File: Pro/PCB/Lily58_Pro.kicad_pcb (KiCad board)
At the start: 2 copper layers, 142.5 x 106.3 mm, 87 parts, among them J1 LED, J2 4PIN, J3 OLED, P1 i2c_pin, P2 i2c_pin, SW1 SW_PUSH, SW10 SW_PUSH, SW11 SW_PUSH, SW12 SW_PUSH, SW13 SW_PUSH, SW14 SW_PUSH, SW15 SW_PUSH, SW16 SW_PUSH, SW17 SW_PUSH, SW18 SW_PUSH, SW19 SW_PUSH, SW2 SW_PUSH, SW20 SW_PUSH, SW21 SW_PUSH, SW22 SW_PUSH, SW23 SW_PUSH, SW24 SW_PUSH, SW25 SW_PUSH, SW26 SW_PUSH, SW27 SW_PUSH, SW28 SW_PUSH, SW29 SW_PUSH, SW3 SW_PUSH, SW4 SW_PUSH, SW5 SW_PUSH, SW6 SW_PUSH, SW7 SW_PUSH, SW8 SW_PUSH, SW9 SW_PUSH, U1 ProMicro

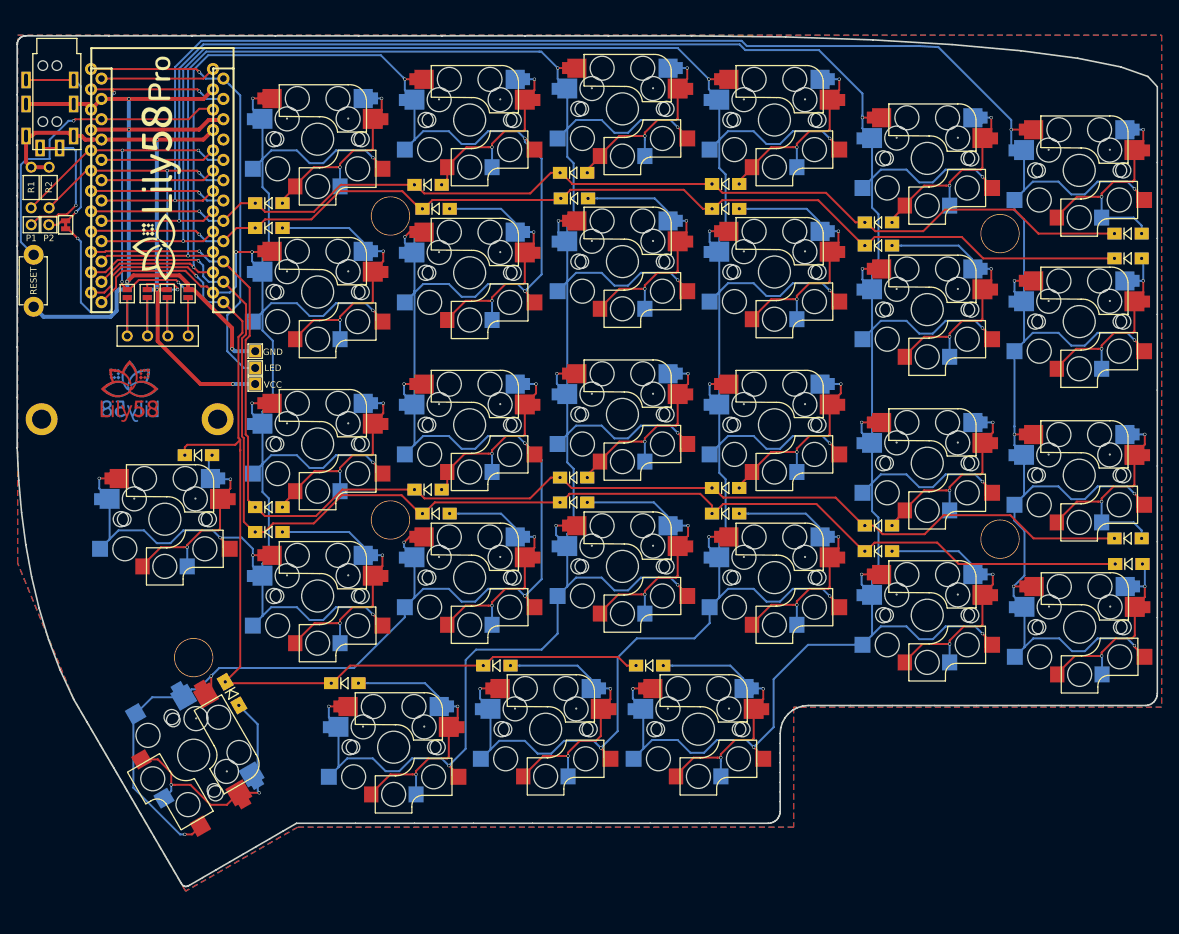
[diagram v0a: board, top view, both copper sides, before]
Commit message: Update footprints a bit, remove some DRC errors (at least we have less of the).
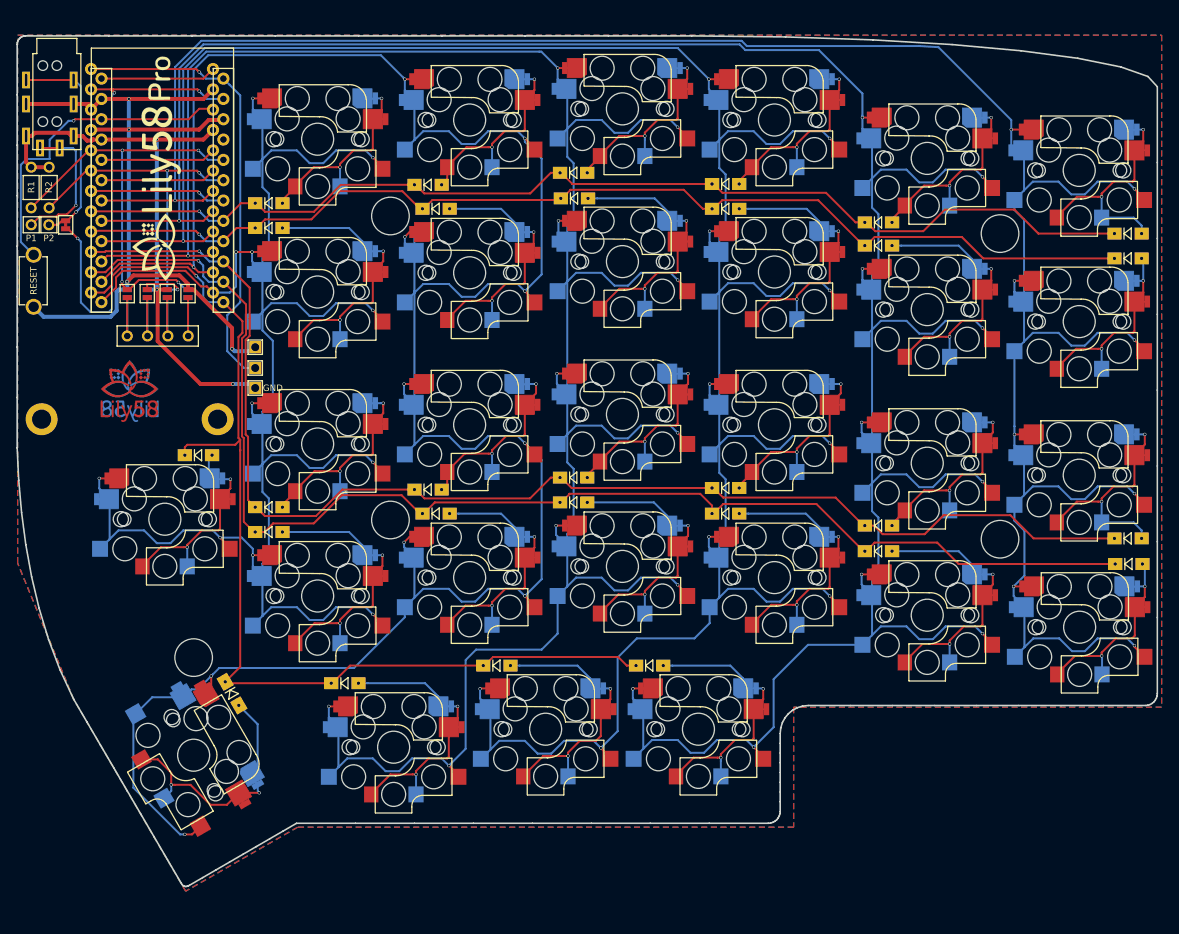
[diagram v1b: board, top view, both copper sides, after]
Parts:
- SW1, SW10, SW11, SW12, SW13, SW14, SW15, SW16, SW17, SW18, SW19, SW2, SW20, SW21, SW22, SW23, SW24, SW25, SW26, SW27, SW28, SW29, SW3, SW4, SW5, SW6, SW7, SW8, SW9: footprint Lily58-footprint:CherryMX_KailhLowProfile_Hotswap_edge -> Lily58-footprint:CherryMX_KailhLowProfile_Hotswap_edge_fixed

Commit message: Add another switch.
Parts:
- added D30: D, Lily58-footprint:Diode_SOD123, F.Cu at (180.7, 121.0)
- added SW30: SW_PUSH, Lily58-footprint:CherryMX_KailhLowProfile_Hotswap, F.Cu at (187.0, 129.0)
- SW1, SW10, SW11, SW12, SW13, SW14, SW15, SW16, SW17, SW18, SW19, SW2, SW20, SW21, SW22, SW23, SW24, SW25, SW27, SW28, SW29, SW3, SW4, SW5, SW6, SW7, SW8, SW9: footprint Lily58-footprint:CherryMX_KailhLowProfile_Hotswap_edge_fixed -> Lily58-footprint:CherryMX_KailhLowProfile_Hotswap
- SW26: footprint Lily58-footprint:CherryMX_KailhLowProfile_Hotswap_edge_fixed -> Lily58-footprint:CherryMX_KailhLowProfile_Hotswap_1.5
- moved SW26 3.22 mm to (106.0, 130.1)
- moved SW27 2.16 mm to (127.9, 126.4), turned to 15 degrees
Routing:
- net col4: track 319.5 -> 254.7 mm, vias 11 -> 10
- net col3: track 319.9 -> 260.8 mm, vias 11 -> 10
- net Net-(D27-Pad2): track 37.1 -> 4.30 mm, vias 2 -> 1
- net Net-(D26-Pad2): track 35.0 -> 4.70 mm, vias 2 -> 1
- net (no net): track 0.00 -> 4.64 mm
- net Net-(D30-Pad2): track 0.00 -> 3.84 mm, vias 0 -> 1
- net col0: track 304.4 -> 308.0 mm, vias 9 -> 10

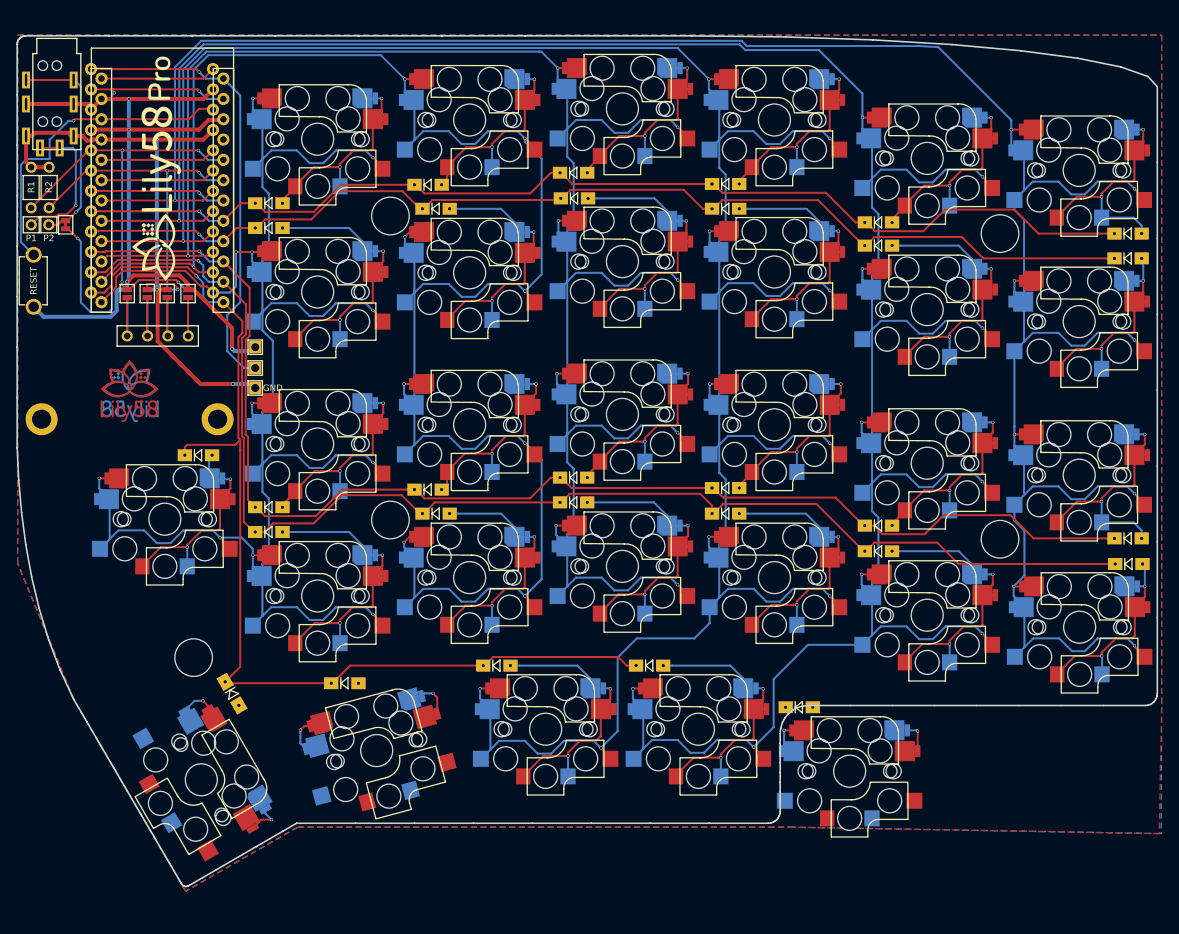
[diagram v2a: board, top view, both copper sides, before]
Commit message: Replace Edeg-Cut with new one.
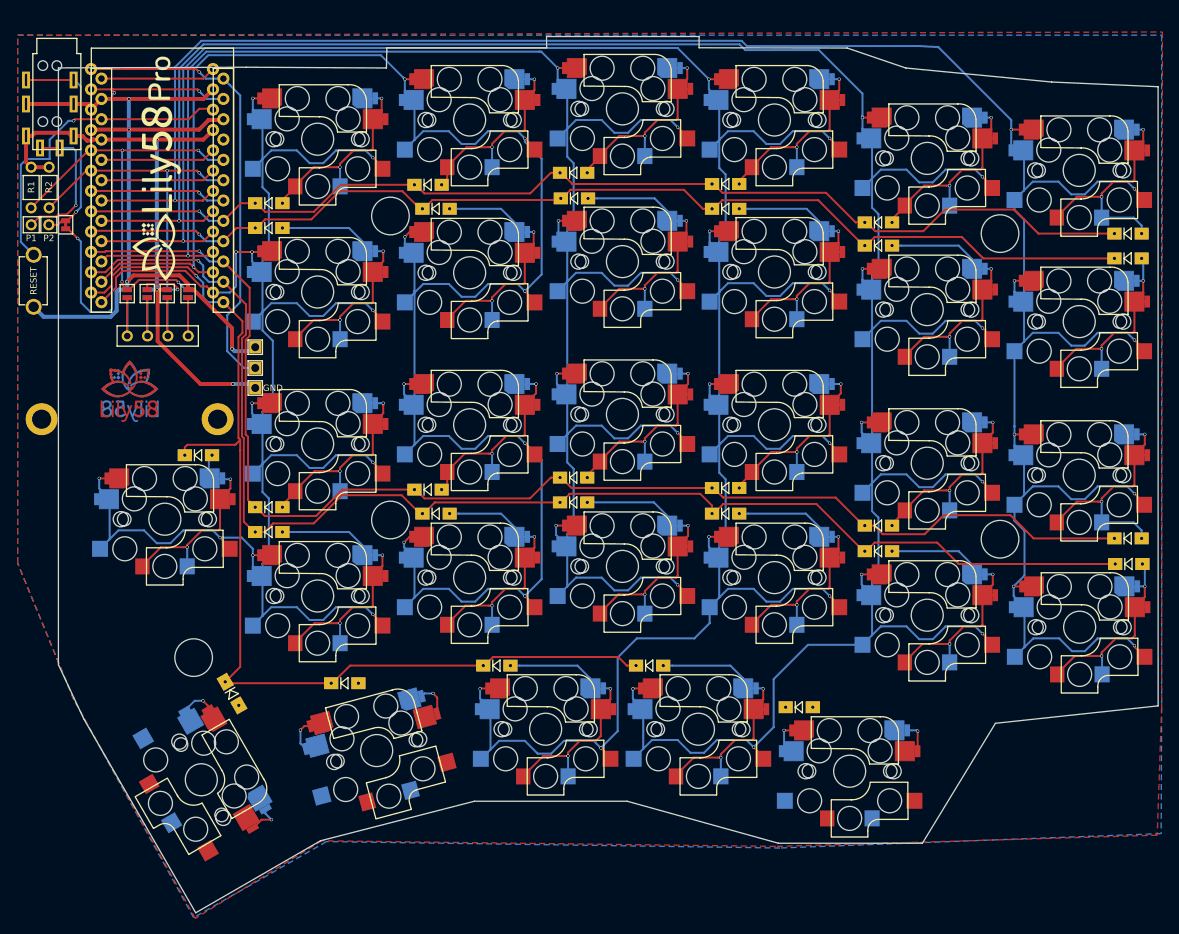
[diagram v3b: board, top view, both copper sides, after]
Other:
- board size 142.5 x 106.3 mm -> 137.5 x 109.5 mm

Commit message: Add rotary encoder, update pcb WIP.
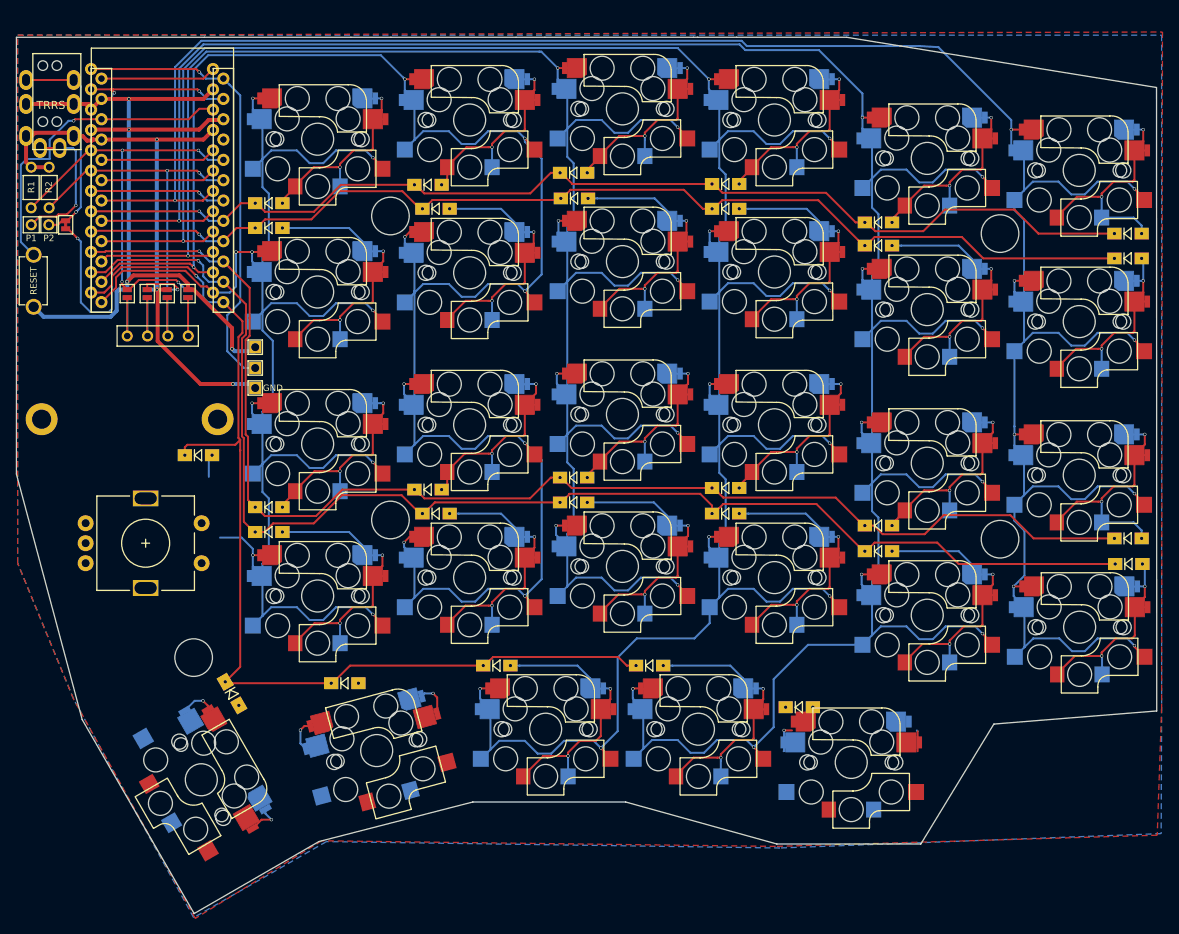
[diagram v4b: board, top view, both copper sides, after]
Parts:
- removed G*** (x2): LOGO, Lily58-footprint:lily58_logo_2
- removed G*** (x2): LOGO, Lily58-footprint:lily58_logo_Pro
- J2: footprint Lily58-footprint:MJ-4PP-9 -> Lily58-footprint:MJ-4PP-9_rev3
- SW25: value SW_PUSH -> Rotary_Encoder_Switch; footprint Lily58-footprint:CherryMX_KailhLowProfile_Hotswap -> Lily58-footprint:RotaryEncoder_Alps_EC11E-Switch_Vertical_H20mm-keebio_modified
- moved SW25 3.84 mm to (99.0, 100.5)
- moved SW30 1.12 mm to (187.2, 127.9)
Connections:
- D25 pad 2: Net-(D25-Pad2) -> SW25B
- P1 pad 1: Net-(J2-Pad4) -> (no net)
- SW1 pad 1: col5 -> SW25A
- SW13 pad 1: col5 -> SW25A
- SW19 pad 1: col5 -> SW25A
- SW7 pad 1: col5 -> SW25A
- U1 pad 13: col5 -> SW25A
- U1 pad 19: Net-(U1-Pad19) -> ENCB
- U1 pad 20: Net-(U1-Pad20) -> ENCA
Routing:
- net col5: track 235.9 -> 0.00 mm, vias 11 -> 0
- net SW25A: track 0.00 -> 204.1 mm, vias 0 -> 9
- net Net-(D25-Pad2): track 28.2 -> 0.00 mm, vias 2 -> 0
- net Net-(J2-Pad4): track 17.9 -> 0.00 mm, vias 1 -> 0
- net (no net): track 4.64 -> 22.6 mm, vias 0 -> 1
- net Net-(U1-Pad20): track 14.4 -> 0.00 mm
- net Net-(U1-Pad19): track 14.4 -> 0.00 mm
- net ENCB: track 0.00 -> 14.4 mm
- net ENCA: track 0.00 -> 14.4 mm
- net SW25B: track 0.00 -> 2.87 mm
- net Net-(D30-Pad2): track 3.84 -> 2.64 mm, vias 1 -> 0
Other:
- board size 137.5 x 109.5 mm -> 142.5 x 109.5 mm

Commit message: Working on routing
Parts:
- moved J2 46.4 mm to (88.0, 85.7), turned to 90 degrees
- moved P1 31.1 mm to (103.2, 85.7)
- moved P2 31.1 mm to (105.4, 85.7)
- moved R1 31.1 mm to (103.2, 81.0)
- moved R2 31.1 mm to (105.4, 81.0)
- moved W1 31.1 mm to (107.5, 85.7)
- moved RSW1 11.0 mm to (90.0, 77.5), turned to 270 degrees
- moved TH1 9.86 mm to (91.0, 93.5)
- moved TH2 8.56 mm to (107.0, 93.5)
- moved D25 7.63 mm to (107.0, 97.0)
- moved SW25 4.12 mm to (100.0, 104.5)
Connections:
- P1 pad 1: (no net) -> /i2c_c
- P2 pad 1: Net-(J2-Pad3) -> /i2c_d
- W1 pad 2: Net-(J2-Pad3) -> /i2c_d
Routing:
- net ENCB: track 14.4 -> 73.1 mm, vias 0 -> 1
- net ENCA: track 14.4 -> 69.0 mm, vias 0 -> 1
- net GND: track 103.0 -> 133.4 mm
- net Net-(J2-Pad3): track 26.6 -> 0.00 mm, vias 1 -> 0
- net /i2c_d: track 0.00 -> 24.6 mm
- net (no net): track 22.6 -> 4.64 mm, vias 1 -> 0
- net DATA: track 59.7 -> 45.3 mm, vias 3 -> 2
- net RESET: track 40.3 -> 51.2 mm, vias 1 -> 0
- net SDA: track 53.8 -> 43.6 mm
- net /i2c_c: track 0.00 -> 6.02 mm
- net SCL: track 45.4 -> 39.5 mm
- net SW25B: track 2.87 -> 5.79 mm
- net SW25A: track 204.1 -> 206.1 mm
- net row4: track 132.6 -> 130.6 mm
- net VCC: track 72.8 -> 70.9 mm

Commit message: Working on routing 2
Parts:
- moved W1 17.2 mm to (94.0, 75.0), turned to 270 degrees
- moved P2 8.07 mm to (102.7, 78.1), turned to 270 degrees
- moved R2 7.98 mm to (98.0, 78.1), turned to 0 degrees
- moved P1 5.42 mm to (102.7, 80.3), turned to 270 degrees
- moved R1 5.20 mm to (98.0, 80.3), turned to 0 degrees
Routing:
- net SDA: track 43.6 -> 57.0 mm
- net SCL: track 39.5 -> 50.8 mm
- net VCC: track 70.9 -> 76.5 mm
- net /i2c_d: track 24.6 -> 29.6 mm
- net ENCA: track 69.0 -> 73.0 mm
- net /i2c_c: track 6.02 -> 9.85 mm
- net DATA: track 45.3 -> 48.8 mm, vias 2 -> 3

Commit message: Routing completed.
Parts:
- moved D30 1.61 mm to (180.9, 119.4)
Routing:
- net col4: track 254.7 -> 311.0 mm, vias 10 -> 11
- net col3: track 260.8 -> 314.7 mm, vias 10 -> 11
- net col0: track 308.0 -> 358.0 mm, vias 10 -> 11
- net Net-(D30-Pad2): track 2.64 -> 37.0 mm, vias 0 -> 2
- net Net-(D26-Pad2): track 4.70 -> 36.4 mm, vias 1 -> 2
- net Net-(D27-Pad2): track 4.30 -> 32.8 mm, vias 1 -> 2
- net row4: track 130.6 -> 152.5 mm
- net (no net): track 4.64 -> 0.00 mm
- net SCL: track 50.8 -> 50.1 mm

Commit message: Update shape
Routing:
- net GND: track 133.6 -> 128.0 mm
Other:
- board size 142.5 x 109.5 mm -> 137.5 x 109.5 mm
